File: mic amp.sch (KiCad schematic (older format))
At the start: 26 parts, among them P1 BNC, SW1 DPDT, U1 LME49710, U2 LF356

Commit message: ENH: Updated through-hole version
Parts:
- removed MIC1: 5P_miniDIN, symbol 5P_miniDIN
- removed P1: BNC, symbol BNC
- removed PWR1: PWR, symbol 4P_miniDIN_PWR
- removed SW1: DPDT, symbol DPDT
- removed U1: LME49710, symbol LME49710
- added J1, J8: CONN_01X02, Conn_PinSocket_2.54mm:PinSocket_1x02_P2.54mm_Vertical, symbol CONN_01X02
- added J2: CONN_01X01, Conn_PinSocket_2.54mm:PinSocket_1x01_P2.54mm_Vertical, symbol CONN_01X01
- added J3: CONN_01X03, Conn_PinSocket_2.54mm:PinSocket_1x03_P2.54mm_Vertical, symbol CONN_01X03
- added J4, J5, J6, J7: CONN_01X01, MountingHole:MountingHole_3.2mm_M3, symbol CONN_01X01
- added J9: CONN_01X05, Conn_PinSocket_2.54mm:PinSocket_1x05_P2.54mm_Vertical, symbol CONN_01X05
- added U1: LF356, Package_DIP:DIP-8_W7.62mm_LongPads, symbol LF356
- C1: value 47nFM -> 68nF metal film; footprint (none) -> Capacitor_THT:C_Rect_L7.2mm_W3.5mm_P5.00mm_FKS2_FKP2_MKS2_MKP2; symbol C -> C-RESCUE-mic_amp
- C10, C11: value 1uFMF -> 1uF; footprint (none) -> custom:C_Rect_L5.5mm_W3.15mm_P2.50mm; symbol C -> C-RESCUE-mic_amp
- C12, C13, C22, C23: value 0.1uFC -> 0.1uF; footprint (none) -> custom:C_Rect_L4.5mm_W3.15mm_P2.50mm; symbol C -> C-RESCUE-mic_amp
- C31: value 47pFM -> 220pF metal film; footprint (none) -> Capacitor_THT:C_Rect_L7.2mm_W4.5mm_P5.00mm_FKS2_FKP2_MKS2_MKP2; symbol C -> C-RESCUE-mic_amp
- C5: value 0.1uFC -> 0.1uF; footprint (none) -> custom:C_Rect_L5.5mm_W3.15mm_P2.50mm; symbol C -> C-RESCUE-mic_amp
- C6, C7: value 100uFE -> 100uF; footprint (none) -> Capacitor_THT:CP_Radial_D10.0mm_P5.00mm
- R1: value 220K -> 49.9k; footprint (none) -> Resistor_THT:R_Axial_DIN0207_L6.3mm_D2.5mm_P10.16mm_Horizontal; symbol R -> R-RESCUE-mic_amp
- R10, R13, R24: footprint (none) -> Resistor_THT:R_Axial_DIN0207_L6.3mm_D2.5mm_P10.16mm_Horizontal; symbol R -> R-RESCUE-mic_amp
- R11, R22, R23: footprint (none) -> Resistor_THT:R_Axial_DIN0204_L3.6mm_D1.6mm_P5.08mm_Horizontal; symbol R -> R-RESCUE-mic_amp
- R31: value 49.9K -> 10k; footprint (none) -> Resistor_THT:R_Axial_DIN0207_L6.3mm_D2.5mm_P10.16mm_Horizontal; symbol R -> R-RESCUE-mic_amp
- U2: footprint (none) -> Package_DIP:DIP-8_W7.62mm_LongPads
- VREG1: footprint (none) -> Package_TO_SOT_THT:TO-92_Inline_Narrow_Oval
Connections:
- wire segments 78 -> 64
- no-connect marks 1 -> 8
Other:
- moved on the sheet: C11

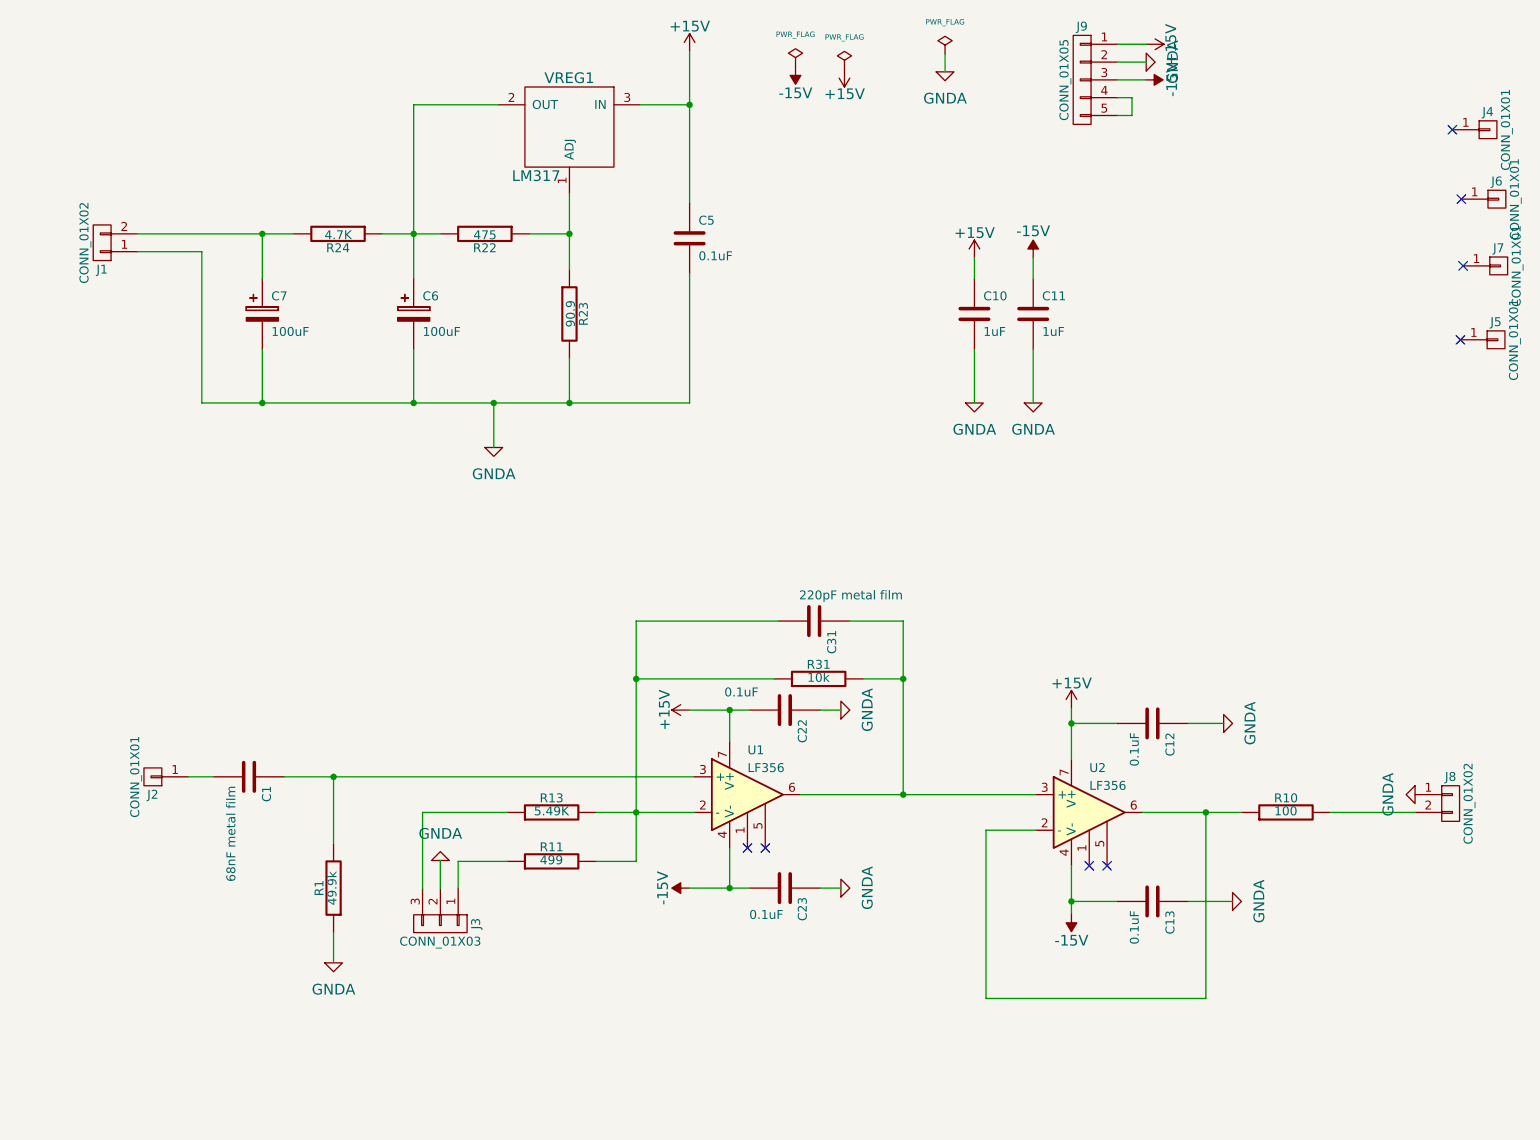
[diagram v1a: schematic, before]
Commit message: Through-hole version of mic amp
Printed via OSH park. Part list availbale via Mouser (see 171218 mic amp
project). Designed to fit a Hammond enclosure that accomodates 75mm wide
PCBs.
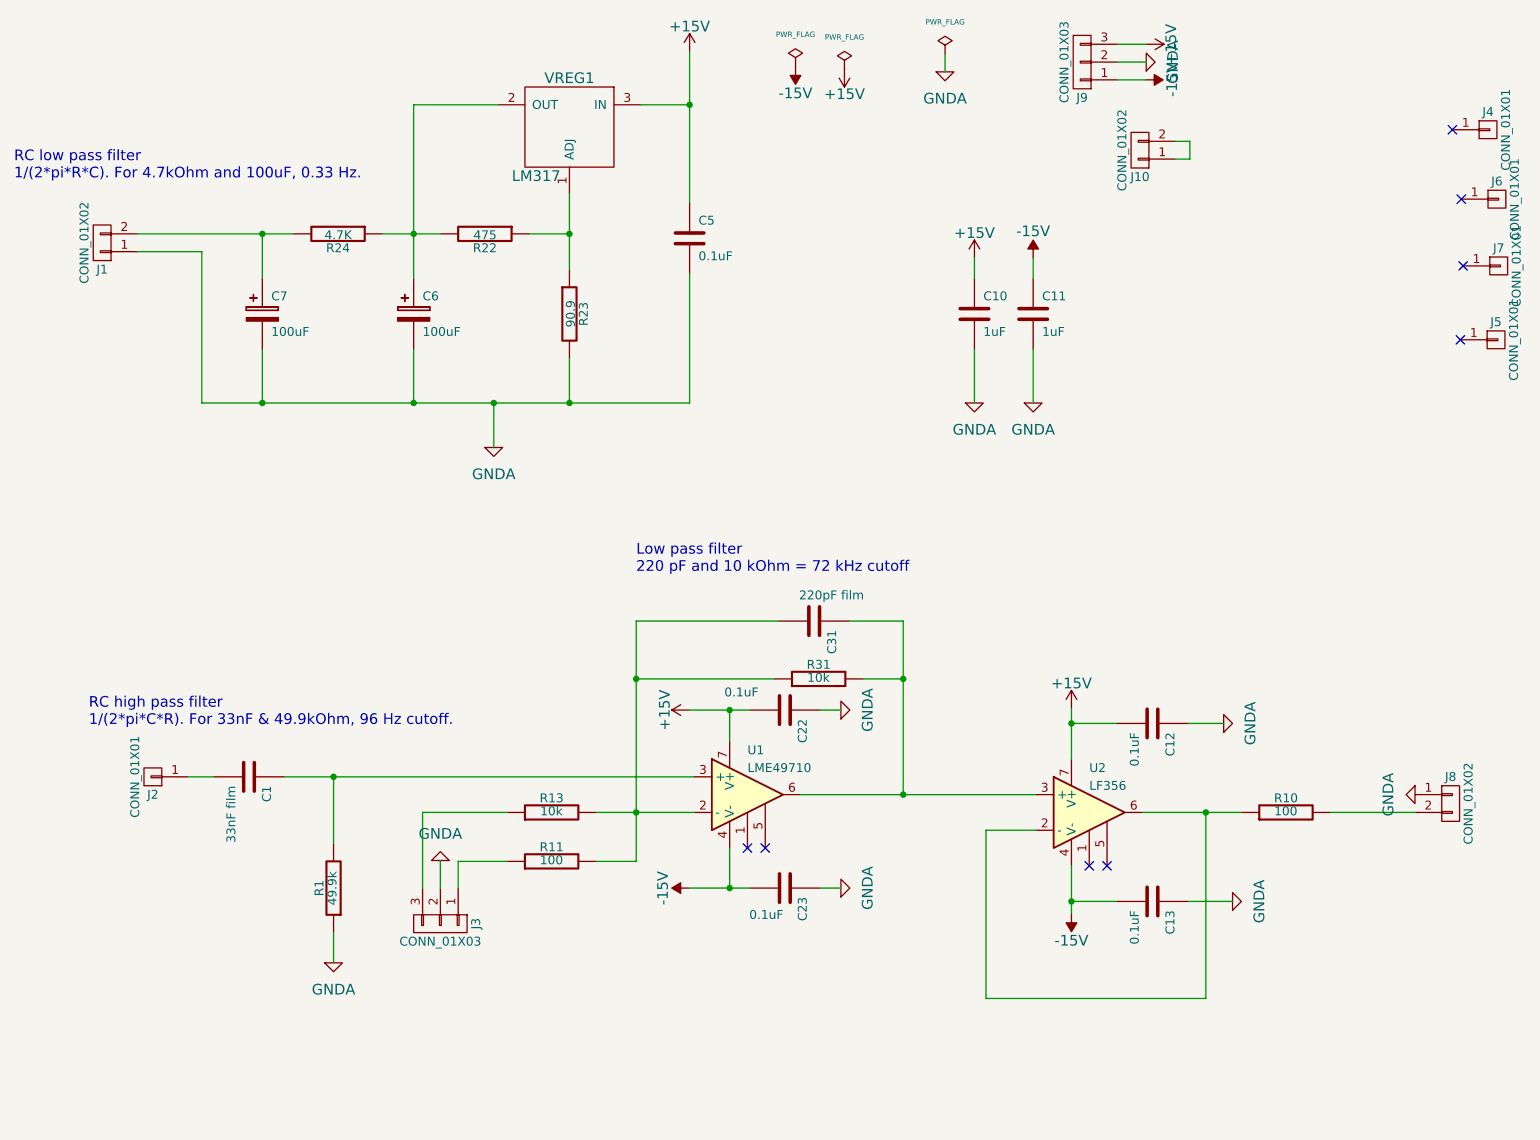
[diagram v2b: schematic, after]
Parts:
- removed J9: CONN_01X05, Conn_PinSocket_2.54mm:PinSocket_1x05_P2.54mm_Vertical, symbol CONN_01X05
- added J10: CONN_01X02, Conn_PinSocket_2.54mm:PinSocket_1x02_P2.54mm_Vertical, symbol CONN_01X02
- added J9: CONN_01X03, Conn_PinSocket_2.54mm:PinSocket_1x03_P2.54mm_Vertical, symbol CONN_01X03
- C1: value 68nF metal film -> 33nF film; footprint Capacitor_THT:C_Rect_L7.2mm_W3.5mm_P5.00mm_FKS2_FKP2_MKS2_MKP2 -> Capacitor_THT:C_Rect_L7.2mm_W8.5mm_P5.00mm_FKP2_FKP2_MKS2_MKP2
- C10, C11: footprint custom:C_Rect_L5.5mm_W3.15mm_P2.50mm -> custom:C_Rect_L5.5mm_W4.0mm_P2.50mm
- C12, C13, C22, C23: footprint custom:C_Rect_L4.5mm_W3.15mm_P2.50mm -> custom:C_Rect_L4.0mm_W3.5mm_P2.50mm
- C31: value 220pF metal film -> 220pF film
- C5: footprint custom:C_Rect_L5.5mm_W3.15mm_P2.50mm -> custom:C_Rect_L4.0mm_W3.5mm_P2.50mm
- R1, R10, R24, R31: footprint Resistor_THT:R_Axial_DIN0207_L6.3mm_D2.5mm_P10.16mm_Horizontal -> Resistor_THT:R_Axial_DIN0207_L6.3mm_D2.5mm_P7.62mm_Horizontal
- R11: value 499 -> 100; footprint Resistor_THT:R_Axial_DIN0204_L3.6mm_D1.6mm_P5.08mm_Horizontal -> Resistor_THT:R_Axial_DIN0207_L6.3mm_D2.5mm_P7.62mm_Horizontal
- R13: value 5.49K -> 10k; footprint Resistor_THT:R_Axial_DIN0207_L6.3mm_D2.5mm_P10.16mm_Horizontal -> Resistor_THT:R_Axial_DIN0207_L6.3mm_D2.5mm_P7.62mm_Horizontal
- R22, R23: footprint Resistor_THT:R_Axial_DIN0204_L3.6mm_D1.6mm_P5.08mm_Horizontal -> Resistor_THT:R_Axial_DIN0207_L6.3mm_D2.5mm_P7.62mm_Horizontal
- U1: value LF356 -> LME49710
- VREG1: footprint Package_TO_SOT_THT:TO-92_Inline_Narrow_Oval -> Package_TO_SOT_THT:TO-92_Inline_Wide
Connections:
- net +15V: now also J9.3 (P3)
- net -15V: now also J9.1 (P1)
- net GNDA: now also J9.2 (P2)
- new net: J10.1 (P1), J10.2 (P2)
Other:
- note added: "Low pass filter\n220 pF and 10 kOhm = 72 kHz cutoff"
- note added: "RC high pass filter\n1/(2*pi*C*R). For 33nF & 49.9kOhm, 96 Hz cutoff."
- note added: "RC low pass filter\n1/(2*pi*R*C). For 4.7kOhm and 100uF, 0.33 Hz."
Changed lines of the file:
@@
 F 0 "VREG1" H 3775 1725 60  0000 C CNN
 F 1 "LM317" H 3825 1175 60  0000 L CNN
-F 2 "Package_TO_SOT_THT:TO-92_Inline_Narrow_Oval" H 3775 1425 60  0001 C CNN
+F 2 "Package_TO_SOT_THT:TO-92_Inline_Wide" H 3775 1425 60  0001 C CNN
 F 3 "" H 3775 1425 60  0000 C CNN
 	1    3775 1425
@@
 F 0 "R23" V 3855 2450 50  0000 C CNN
 F 1 "90.9" V 3782 2451 50  0000 C CNN
-F 2 "Resistor_THT:R_Axial_DIN0204_L3.6mm_D1.6mm_P5.08mm_Horizontal" V 3705 2450 30  0001 C CNN
+F 2 "Resistor_THT:R_Axial_DIN0207_L6.3mm_D2.5mm_P7.62mm_Horizontal" V 3705 2450 30  0001 C CNN
 F 3 "" H 3775 2450 30  0000 C CNN
 	1    3775 2450
@@
 F 0 "R22" V 3380 2000 50  0000 C CNN
 F 1 "475" V 3307 2001 50  0000 C CNN
-F 2 "Resistor_THT:R_Axial_DIN0204_L3.6mm_D1.6mm_P5.08mm_Horizontal" V 3230 2000 30  0001 C CNN
+F 2 "Resistor_THT:R_Axial_DIN0207_L6.3mm_D2.5mm_P7.62mm_Horizontal" V 3230 2000 30  0001 C CNN
 F 3 "" H 3300 2000 30  0000 C CNN
 	1    3300 2000
@@
 F 0 "R24" V 2555 2000 50  0000 C CNN
 F 1 "4.7K" V 2482 2001 50  0000 C CNN
-F 2 "Resistor_THT:R_Axial_DIN0207_L6.3mm_D2.5mm_P10.16mm_Horizontal" V 2405 2000 30  0001 C CNN
+F 2 "Resistor_THT:R_Axial_DIN0207_L6.3mm_D2.5mm_P7.62mm_Horizontal" V 2405 2000 30  0001 C CNN
 F 3 "" H 2475 2000 30  0000 C CNN
 	1    2475 2000
@@
 F 0 "C5" H 4500 2125 50  0000 L CNN
 F 1 "0.1uF" H 4500 1925 50  0000 L CNN
-F 2 "custom:C_Rect_L5.5mm_W3.15mm_P2.50mm" H 4488 1875 30  0001 C CNN
+F 2 "custom:C_Rect_L4.0mm_W3.5mm_P2.50mm" H 4488 1875 30  0001 C CNN
 F 3 "" H 4450 2025 60  0000 C CNN
 	1    4450 2025
@@
 F 0 "R1" V 2530 5675 50  0000 C CNN
 F 1 "49.9k" V 2457 5676 50  0000 C CNN
-F 2 "Resistor_THT:R_Axial_DIN0207_L6.3mm_D2.5mm_P10.16mm_Horizontal" V 2380 5675 30  0001 C CNN
+F 2 "Resistor_THT:R_Axial_DIN0207_L6.3mm_D2.5mm_P7.62mm_Horizontal" V 2380 5675 30  0001 C CNN
 F 3 "" H 2450 5675 30  0000 C CNN
 	1    2450 5675
@@
 P 1975 5050
 F 0 "C1" H 2025 5150 50  0000 L CNN
-F 1 "68nF metal film" H 2025 4950 50  0000 L CNN
-F 2 "Capacitor_THT:C_Rect_L7.2mm_W3.5mm_P5.00mm_FKS2_FKP2_MKS2_MKP2" H 2013 4900 30  0001 C CNN
+F 1 "33nF film" H 2025 4950 50  0000 L CNN
+F 2 "Capacitor_THT:C_Rect_L7.2mm_W8.5mm_P5.00mm_FKP2_FKP2_MKS2_MKP2" H 2013 4900 30  0001 C CNN
 F 3 "" H 1975 5050 60  0000 C CNN
 	1    1975 5050
@@
 P 3675 5250
 F 0 "R13" V 3755 5250 50  0000 C CNN
-F 1 "5.49K" V 3682 5251 50  0000 C CNN
-F 2 "Resistor_THT:R_Axial_DIN0207_L6.3mm_D2.5mm_P10.16mm_Horizontal" V 3605 5250 30  0001 C CNN
+F 1 "10k" V 3682 5251 50  0000 C CNN
+F 2 "Resistor_THT:R_Axial_DIN0207_L6.3mm_D2.5mm_P7.62mm_Horizontal" V 3605 5250 30  0001 C CNN
 F 3 "" H 3675 5250 30  0000 C CNN
 	1    3675 5250
@@
 P 3675 5525
 F 0 "R11" V 3755 5525 50  0000 C CNN
-F 1 "499" V 3682 5526 50  0000 C CNN
-F 2 "Resistor_THT:R_Axial_DIN0204_L3.6mm_D1.6mm_P5.08mm_Horizontal" V 3605 5525 30  0001 C CNN
+F 1 "100" V 3682 5526 50  0000 C CNN
+F 2 "Resistor_THT:R_Axial_DIN0207_L6.3mm_D2.5mm_P7.62mm_Horizontal" V 3605 5525 30  0001 C CNN
 F 3 "" H 3675 5525 30  0000 C CNN
 	1    3675 5525
@@
 F 0 "R31" V 5255 4500 50  0000 C CNN
 F 1 "10k" V 5182 4501 50  0000 C CNN
-F 2 "Resistor_THT:R_Axial_DIN0207_L6.3mm_D2.5mm_P10.16mm_Horizontal" V 5105 4500 30  0001 C CNN
+F 2 "Resistor_THT:R_Axial_DIN0207_L6.3mm_D2.5mm_P7.62mm_Horizontal" V 5105 4500 30  0001 C CNN
 F 3 "" H 5175 4500 30  0000 C CNN
 	1    5175 4500
@@
 P 5150 4175
 F 0 "C31" H 5200 4275 50  0000 L CNN
-F 1 "220pF metal film" V 5005 4090 50  0000 L CNN
+F 1 "220pF film" V 5005 4090 50  0000 L CNN
 F 2 "Capacitor_THT:C_Rect_L7.2mm_W4.5mm_P5.00mm_FKS2_FKP2_MKS2_MKP2" H 5188 4025 30  0001 C CNN
 F 3 "" H 5150 4175 60  0000 C CNN
@@
 F 0 "C12" H 7100 4850 50  0000 L CNN
 F 1 "0.1uF" H 7100 4650 50  0000 L CNN
-F 2 "custom:C_Rect_L4.5mm_W3.15mm_P2.50mm" H 7088 4600 30  0001 C CNN
+F 2 "custom:C_Rect_L4.0mm_W3.5mm_P2.50mm" H 7088 4600 30  0001 C CNN
 F 3 "" H 7050 4750 60  0000 C CNN
 	1    7050 4750
@@
 F 0 "C13" H 7100 5850 50  0000 L CNN
 F 1 "0.1uF" H 7100 5650 50  0000 L CNN
-F 2 "custom:C_Rect_L4.5mm_W3.15mm_P2.50mm" H 7088 5600 30  0001 C CNN
+F 2 "custom:C_Rect_L4.0mm_W3.5mm_P2.50mm" H 7088 5600 30  0001 C CNN
 F 3 "" H 7050 5750 60  0000 C CNN
 	1    7050 5750
@@
 F 0 "R10" V 7880 5250 50  0000 C CNN
 F 1 "100" V 7807 5251 50  0000 C CNN
-F 2 "Resistor_THT:R_Axial_DIN0207_L6.3mm_D2.5mm_P10.16mm_Horizontal" V 7730 5250 30  0001 C CNN
+F 2 "Resistor_THT:R_Axial_DIN0207_L6.3mm_D2.5mm_P7.62mm_Horizontal" V 7730 5250 30  0001 C CNN
 F 3 "" H 7800 5250 30  0000 C CNN
 	1    7800 5250
@@
 F 0 "C11" H 6430 2550 50  0000 L CNN
 F 1 "1uF" H 6430 2350 50  0000 L CNN
-F 2 "custom:C_Rect_L5.5mm_W3.15mm_P2.50mm" H 6418 2300 30  0001 C CNN
+F 2 "custom:C_Rect_L5.5mm_W4.0mm_P2.50mm" H 6418 2300 30  0001 C CNN
 F 3 "" H 6380 2450 60  0000 C CNN
 	1    6380 2450
@@
 F 0 "C10" H 6100 2550 50  0000 L CNN
 F 1 "1uF" H 6100 2350 50  0000 L CNN
-F 2 "custom:C_Rect_L5.5mm_W3.15mm_P2.50mm" H 6088 2300 30  0001 C CNN
+F 2 "custom:C_Rect_L5.5mm_W4.0mm_P2.50mm" H 6088 2300 30  0001 C CNN
 F 3 "" H 6050 2450 60  0000 C CNN
 	1    6050 2450
@@
 F 0 "C22" H 5035 4775 50  0000 L CNN
 F 1 "0.1uF" V 4885 4335 50  0000 L CNN
-F 2 "custom:C_Rect_L4.5mm_W3.15mm_P2.50mm" H 5023 4525 30  0001 C CNN
+F 2 "custom:C_Rect_L4.0mm_W3.5mm_P2.50mm" H 5023 4525 30  0001 C CNN
 F 3 "" H 4985 4675 60  0000 C CNN
 	1    4985 4675
@@
 F 0 "C23" H 5035 5775 50  0000 L CNN
 F 1 "0.1uF" V 5135 5475 50  0000 L CNN
-F 2 "custom:C_Rect_L4.5mm_W3.15mm_P2.50mm" H 5023 5525 30  0001 C CNN
+F 2 "custom:C_Rect_L4.0mm_W3.5mm_P2.50mm" H 5023 5525 30  0001 C CNN
 F 3 "" H 4985 5675 60  0000 C CNN
 	1    4985 5675
@@
 P 4775 5150
 F 0 "U1" H 4775 5400 50  0000 L CNN
-F 1 "LF356" H 4775 5300 50  0000 L CNN
+F 1 "LME49710" H 4775 5300 50  0000 L CNN
 F 2 "Package_DIP:DIP-8_W7.62mm_LongPads" H 4825 5200 50  0001 C CNN
 F 3 "" H 4925 5300 50  0001 C CNN
@@
 	-1   0    0    1
 $EndComp
-$Comp
-L CONN_01X05 J9
-U 1 1 5A1E9F7B
-P 6655 1135
-F 0 "J9" H 6655 1435 50  0000 C CNN
-F 1 "CONN_01X05" V 6755 1135 50  0000 C CNN
-F 2 "Conn_PinSocket_2.54mm:PinSocket_1x05_P2.54mm_Vertical" H 6655 1135 50  0001 C CNN
-F 3 "" H 6655 1135 50  0001 C CNN
-	1    6655 1135
-	-1   0    0    -1
-$EndComp
-Wire Wire Line
-	6855 1335 6935 1335
-Wire Wire Line
-	6935 1335 6935 1235
+Wire Wire Line
+	7180 1580 7260 1580
+Wire Wire Line
+	7260 1580 7260 1480
 $Comp
 L CONN_01X01 J2
@@
 $EndComp
 Wire Wire Line
-	6935 1235 6855 1235
+	7260 1480 7180 1480
+Text Notes 1075 4770 0    60   ~ 0
+RC high pass filter\n1/(2*pi*C*R). For 33nF & 49.9kOhm, 96 Hz cutoff.
+Text Notes 655  1700 0    60   ~ 0
+RC low pass filter\n1/(2*pi*R*C). For 4.7kOhm and 100uF, 0.33 Hz.
+Text Notes 4150 3910 0    60   ~ 0
+Low pass filter\n220 pF and 10 kOhm = 72 kHz cutoff
+$Comp
+L CONN_01X03 J9
+U 1 1 5A304C1A
+P 6655 1035
+F 0 "J9" H 6655 1235 50  0000 C CNN
+F 1 "CONN_01X03" V 6755 1035 50  0000 C CNN
+F 2 "Conn_PinSocket_2.54mm:PinSocket_1x03_P2.54mm_Vertical" H 6655 1035 50  0001 C CNN
+F 3 "" H 6655 1035 50  0001 C CNN
+	1    6655 1035
+	-1   0    0    1
+$EndComp
+$Comp
+L CONN_01X02 J10
+U 1 1 5A304E40
+P 6980 1530
+F 0 "J10" H 6980 1680 50  0000 C CNN
+F 1 "CONN_01X02" V 7080 1530 50  0000 C CNN
+F 2 "Conn_PinSocket_2.54mm:PinSocket_1x02_P2.54mm_Vertical" H 6980 1530 50  0001 C CNN
+F 3 "" H 6980 1530 50  0001 C CNN
+	1    6980 1530
+	-1   0    0    1
+$EndComp
 $EndSCHEMATC
